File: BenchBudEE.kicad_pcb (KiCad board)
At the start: 2 copper layers, 1 part

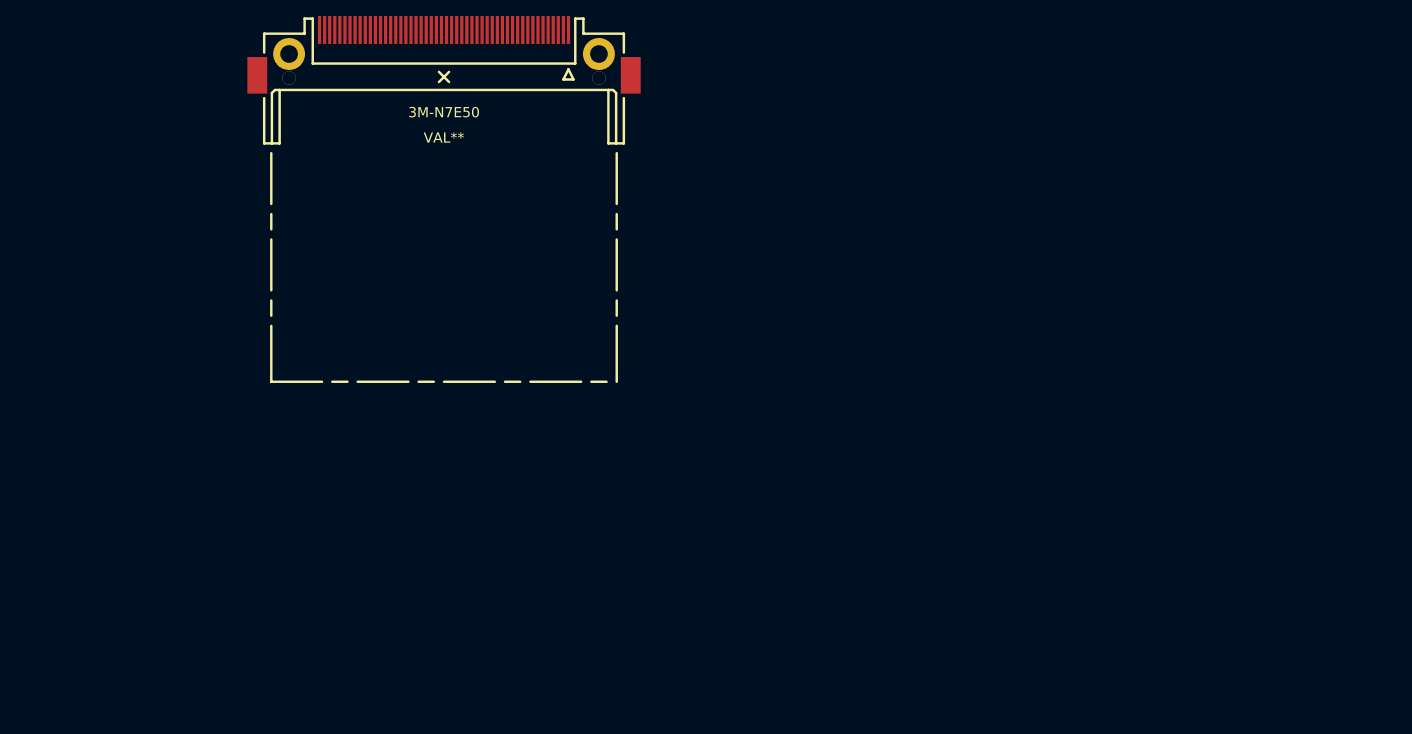
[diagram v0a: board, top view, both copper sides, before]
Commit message: Begin Associating relay Module
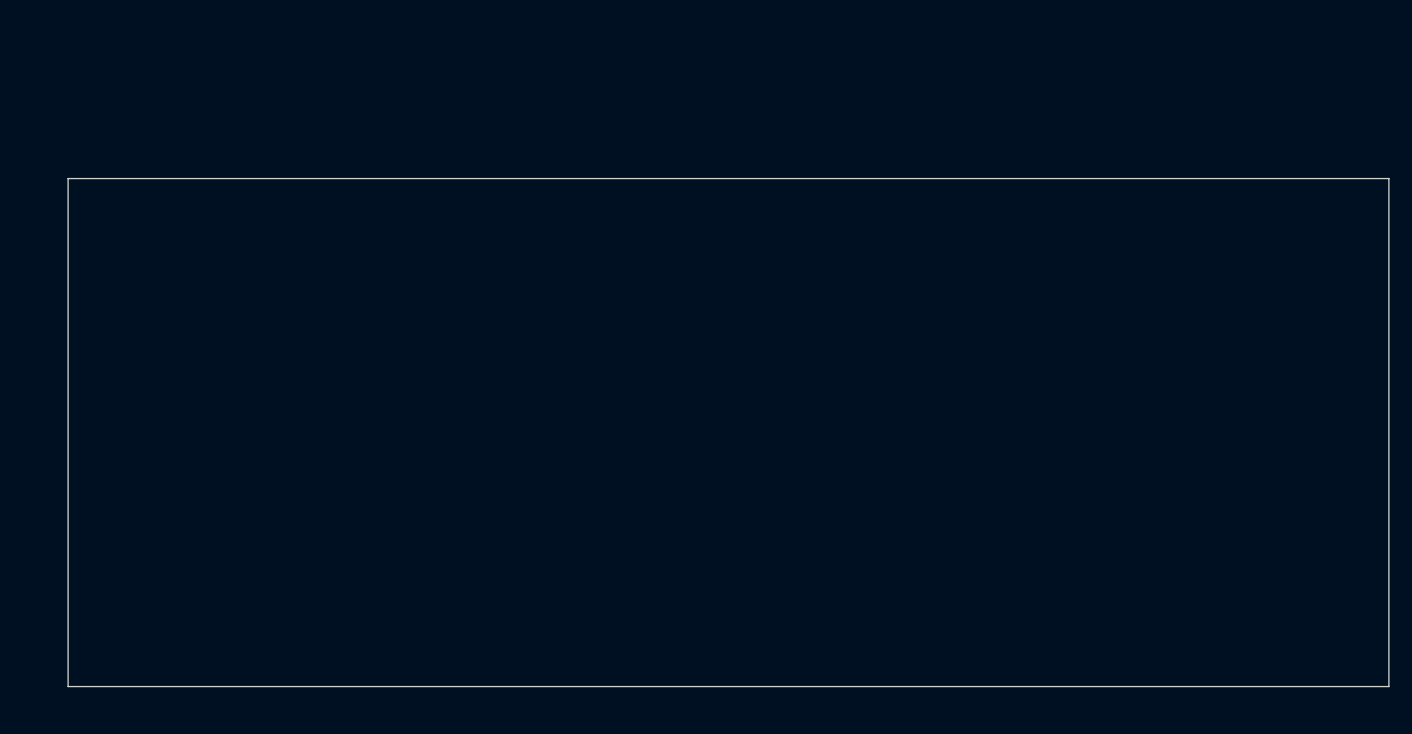
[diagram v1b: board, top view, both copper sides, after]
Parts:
- removed 3M-N7E50: VAL**, connect:3M-N7E50
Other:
- board outline added: 165.1 x 63.5 mm
- copper layers 2 -> 4
- rule trace_min: 0.254 -> 0.127
- rule via_min_drill: 0.508 -> 0.3302
- rule via_min_size: 0.889 -> 0.508

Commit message: Placed Relay Module Components
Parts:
- added D1: LG Q971-KN-1, LEDs:LED-0603, F.Cu at (257.8, 128.8)
- added D2: B130-13-F, BenchBudEE:SMA, B.Cu at (269.7, 126.7)
- added K1: 1461069-5, BenchBudEE:TE-SPDT, F.Cu at (262.9, 124.5)
- added Q1: 2N3904, SMD_Packages:SOT23, B.Cu at (261.6, 131.6)
- added R1: 500, SMD_Packages:SM0805, F.Cu at (250.7, 119.1)
- added R2: 0, SMD_Packages:SM0805, F.Cu at (251.2, 130.3)
- added R3: 200, SMD_Packages:SM0805, F.Cu at (250.2, 124.2)
- added R4: 0, SMD_Packages:SM0805, F.Cu at (270.3, 117.9)
- added R5: 100, SMD_Packages:SM0805, B.Cu at (260.9, 120.4)
- added R6: 0, SMD_Packages:SM0805, F.Cu at (255.0, 132.6)
- added U1: LTV-816S, BenchBudEE:4-SMD, F.Cu at (254.5, 125.2)

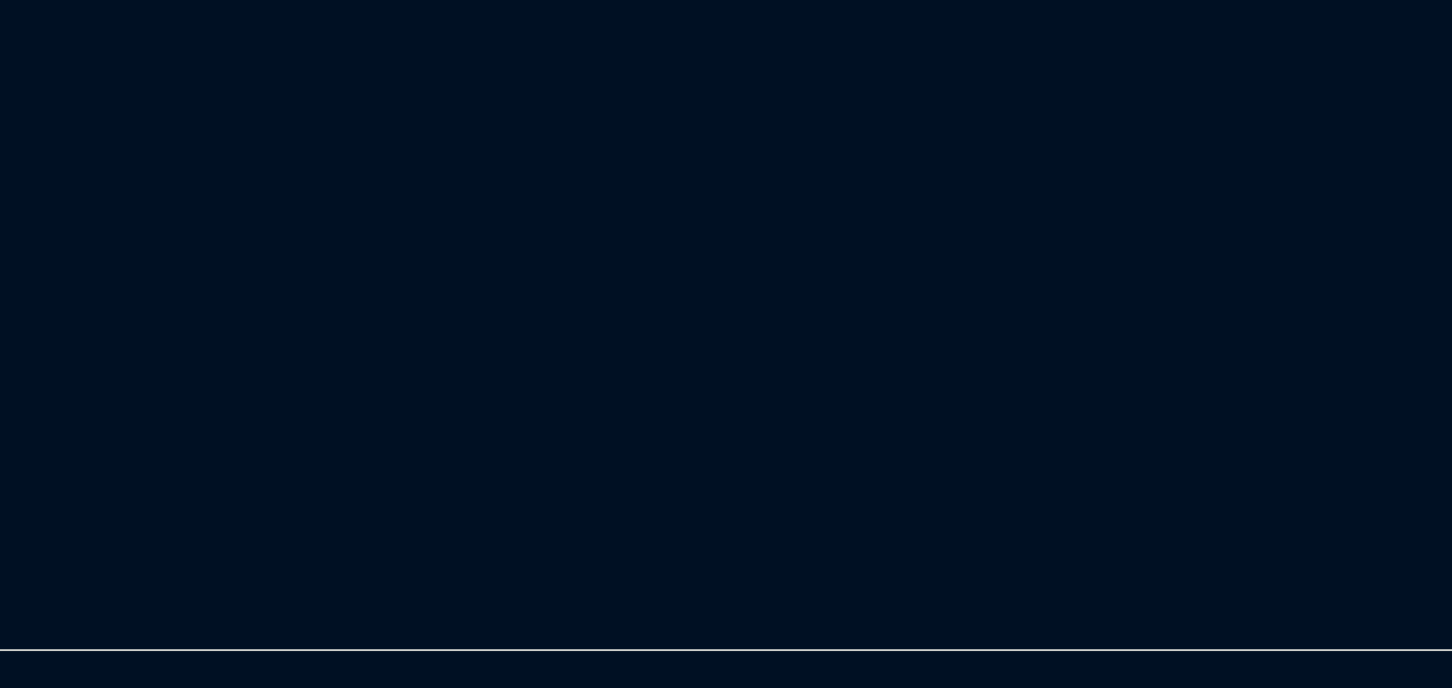
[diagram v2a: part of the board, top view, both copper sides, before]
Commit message: place thermocouple components
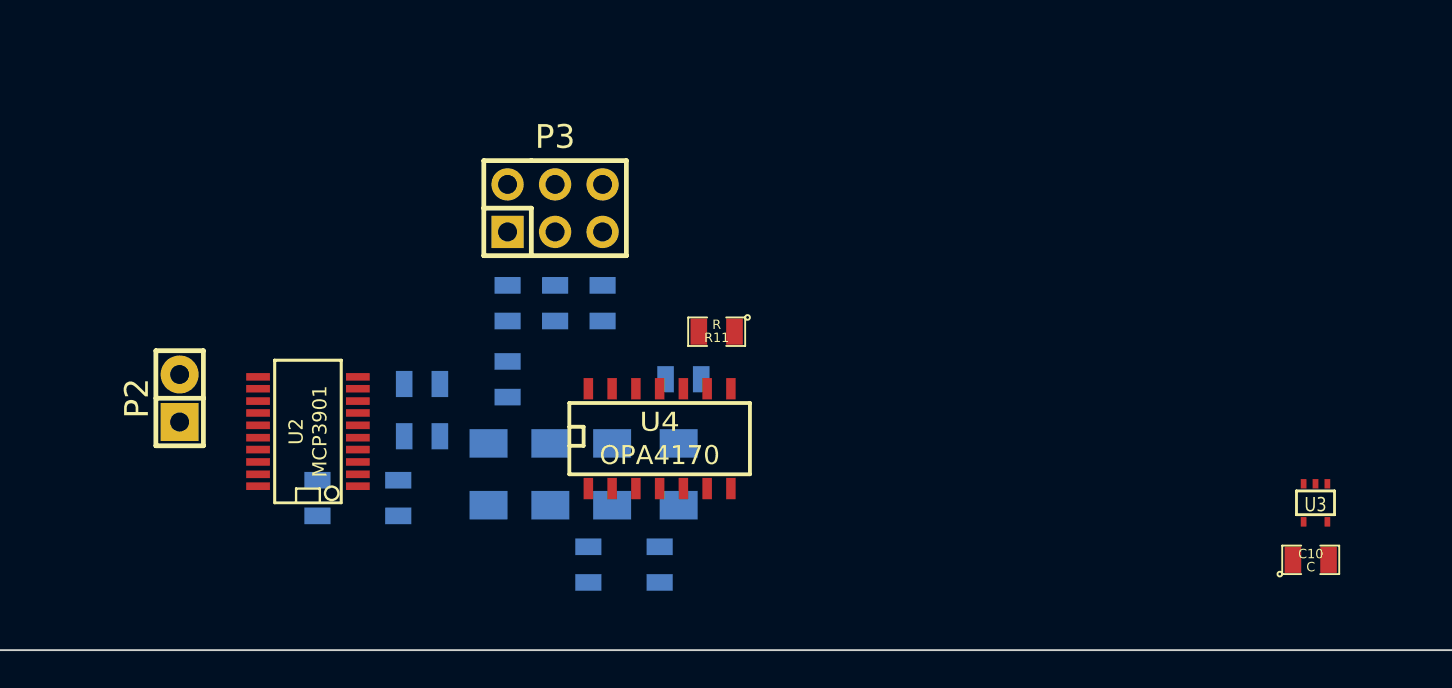
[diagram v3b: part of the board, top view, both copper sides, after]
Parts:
- added C10: C, SMD_Packages:SM0805, F.Cu at (284.5, 173.0)
- added C5: C, SMD_Packages:SM0805, B.Cu at (231.4, 169.7)
- added C6: C, SMD_Packages:SM0805, B.Cu at (235.7, 169.7)
- added C7: C, SMD_Packages:SM0805, B.Cu at (251.0, 163.3)
- added C8: C, SMD_Packages:SM0805, B.Cu at (245.9, 173.2)
- added C9: C, SMD_Packages:SM0805, B.Cu at (249.7, 173.2)
- added P2: CONN_2, Pin_Headers:Pin_Header_Straight_1x02, F.Cu at (224.0, 164.3)
- added P3: CONN_3X2, Pin_Headers:Pin_Header_Straight_2x03, F.Cu at (244.1, 154.2)
- added R10: R, SMD_Packages:SM1206, B.Cu at (240.5, 168.4)
- added R11: R, SMD_Packages:SM0805, F.Cu at (252.7, 160.8)
- added R12: R, SMD_Packages:SM0805, B.Cu at (241.6, 159.3)
- added R13: R, SMD_Packages:SM0805, B.Cu at (241.6, 163.3)
- added R43: R, SMD_Packages:SM0805, B.Cu at (246.6, 159.3)
- added R44: R, SMD_Packages:SM0805, B.Cu at (244.1, 159.3)
- added R47: 0, SMD_Packages:SM0805, B.Cu at (237.0, 163.6)
- added R48: 0, SMD_Packages:SM0805, B.Cu at (237.0, 166.4)
- added R7: R, SMD_Packages:SM1206, B.Cu at (243.8, 168.4)
- added R8: R, SMD_Packages:SM1206, B.Cu at (247.1, 168.4)
- added R9: R, SMD_Packages:SM1206, B.Cu at (250.7, 168.4)
- added U2: MCP3901, SMD_Packages:SSOP20, F.Cu at (230.9, 166.1)
- added U3: LMT84, SMD_Packages:SOT353, F.Cu at (284.7, 169.9)
- added U4: OPA4170, SMD_Packages:SO14E, F.Cu at (249.7, 166.4)

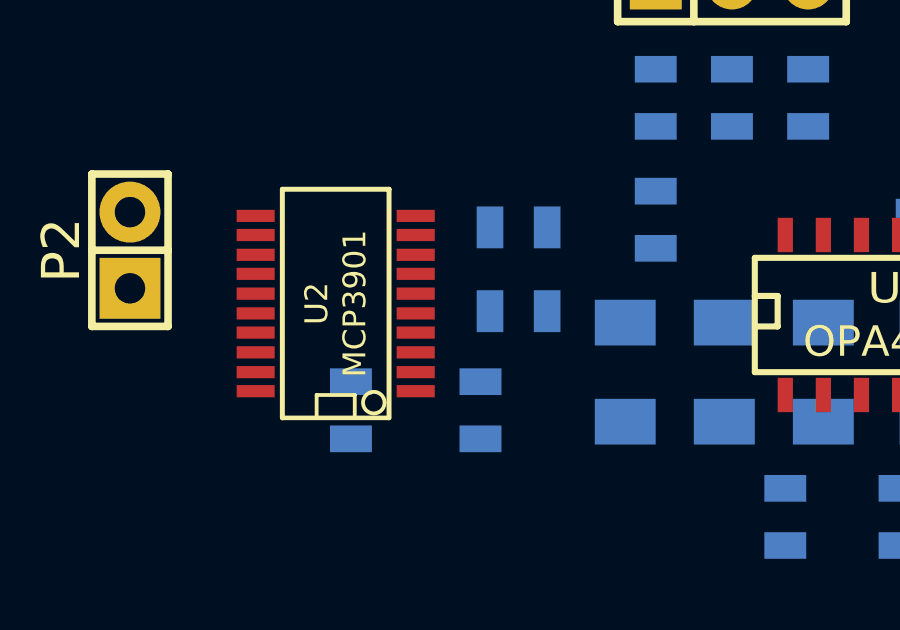
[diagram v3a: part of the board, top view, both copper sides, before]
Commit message: ABOUT TO REPLACE ssop20
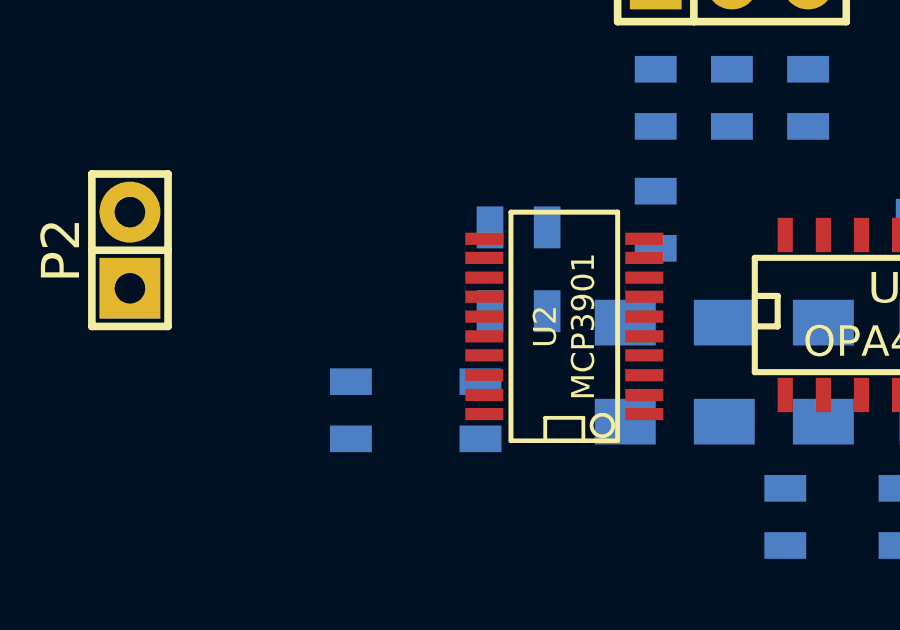
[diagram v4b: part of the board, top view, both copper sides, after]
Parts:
- moved U2 7.66 mm to (238.5, 166.9)
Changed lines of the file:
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@@
     (links 60)
     (no_connects 60)
-    (area 126.949999 114.249999 292.150001 177.850001)
+    (area 126.949999 112.359 292.150001 177.850001)
     (thickness 1.6)
     (drawings 4)
@@
     (mod_text_size 1 1)
     (mod_text_width 0.15)
-    (pad_size 1.905 1.905)
-    (pad_drill 1.27)
+    (pad_size 0.45 1.75)
+    (pad_drill 0)
     (pad_to_mask_clearance 0)
     (aux_axis_origin 0 0)
@@
   )
   (module SMD_Packages:SSOP20 (layer F.Cu)
-    (at 230.886 166.116 90)
+    (at 238.506 166.878 90)
     (descr "SSOP 20 pins")
     (tags "CMS SSOP SMD")

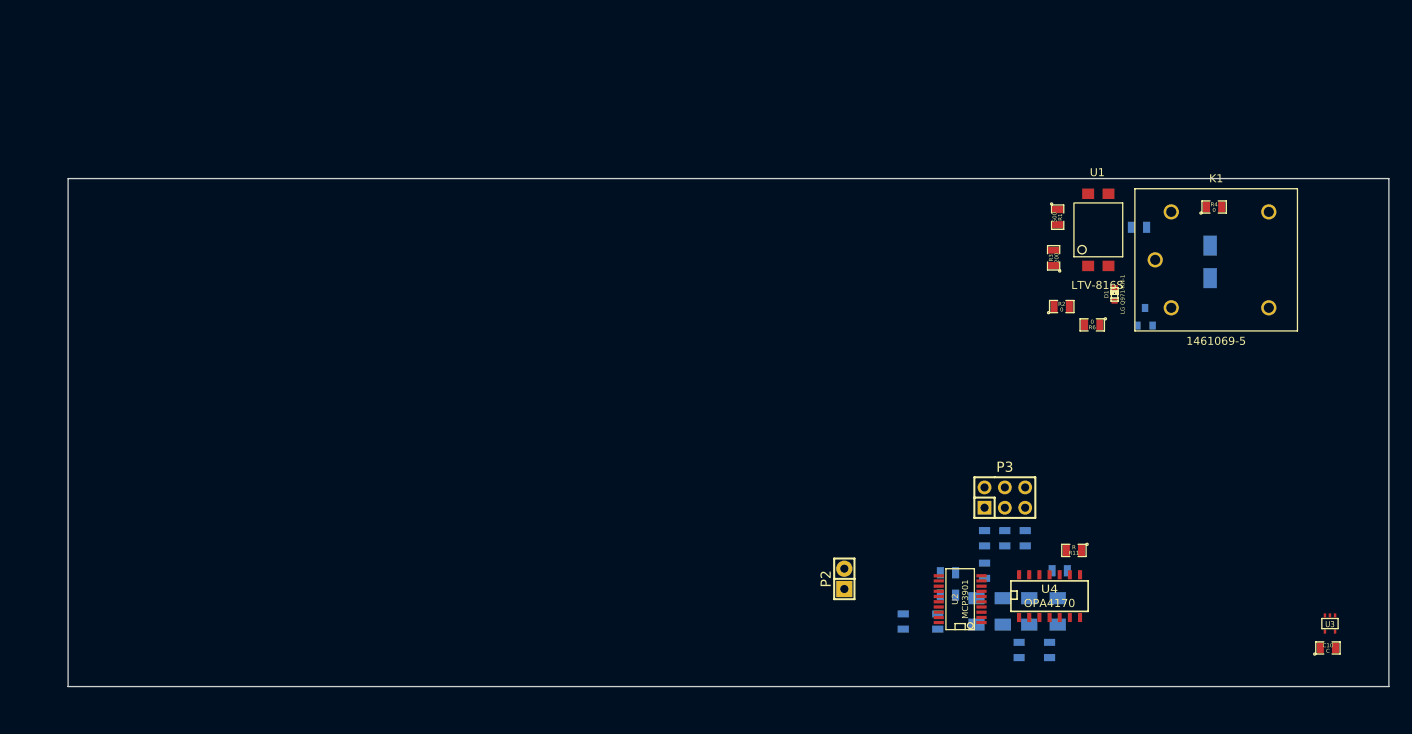
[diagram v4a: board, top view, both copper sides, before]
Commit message: Placement of connectors
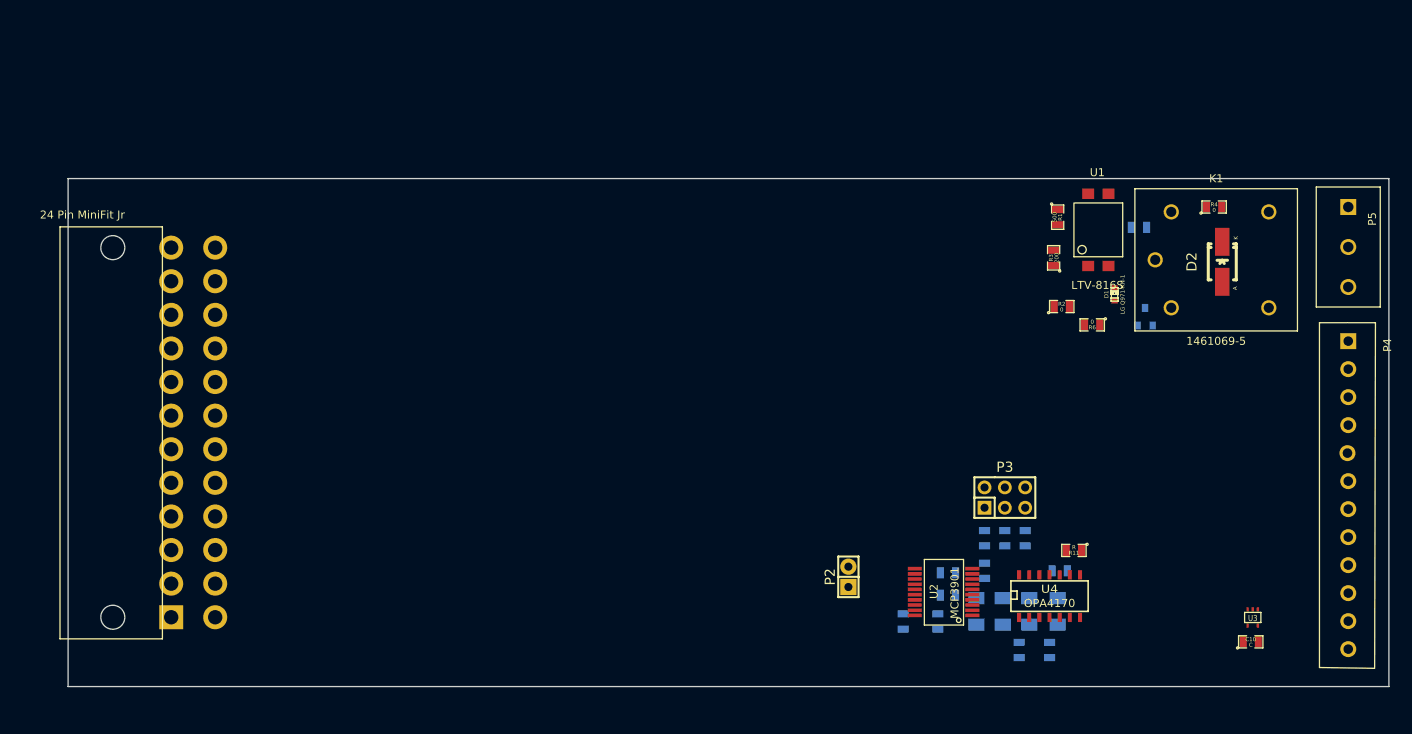
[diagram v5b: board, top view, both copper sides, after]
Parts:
- added P1: 24 Pin MiniFit Jr, BenchBudEE:ATX_Header, F.Cu at (132.6, 122.9)
- added P4: 12 Pin Terminal Block, BenchBudEE:12pinTB, F.Cu at (287.0, 134.6)
- added P5: 3-Pin TB, BenchBudEE:3pinTB, F.Cu at (287.0, 117.9)
- D2: footprint BenchBudEE:SMA -> Diodes_SMD:Diode-SMA_Handsoldering; moved to F.Cu
- U2: footprint SMD_Packages:SSOP20 -> BenchBudEE:SSOP-20_5.3mm
- moved C10 9.68 mm to (274.8, 172.2)
- moved U3 9.68 mm to (275.1, 169.2)
- moved U2 2.54 mm to (240.0, 168.9)
- moved D2 2.54 mm to (271.3, 124.7)
- moved P2 0.57 mm to (224.5, 164.1)
